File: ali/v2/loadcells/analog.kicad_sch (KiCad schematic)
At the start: 40 parts, among them J10 Conn_01x04, J11 Conn_01x04, J12 Conn_01x04, J9 Conn_01x04, U6 ADS124S08

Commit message: Small cleanups
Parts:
- R30: value 1k -> 4.7k; MPN RT0603BRD071KL -> RT0603BRD074K7L
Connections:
- net at C38.2, C39.1, R25.2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: now also D9.1 (A1)
- net at C34.1, C35.2, R22.2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: now also D6.1 (A1)
- net at J9.3 (Pin_3), R23.1: no longer D7.1 (A1)
- net at C35.1, C36.2, R23.2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: now also D7.1 (A1)
- net at J11.2 (Pin_2), R26.1: no longer D10.1 (A1)
- net at J11.3 (Pin_3), R27.1: no longer D11.1 (A1)
- net at J12.2 (Pin_2), R28.1: no longer D12.1 (A1)
- net at C45.1, C47.2, R28.2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: now also D12.1 (A1)
- net at C37.1, C39.2, R24.2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: now also D8.1 (A1)
- net at J10.3 (Pin_3), R25.1: no longer D9.1 (A1)
- net at J12.3 (Pin_3), R29.1: no longer D13.1 (A1)
- net at C43.2, C44.1, R27.2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: now also D11.1 (A1)
- net at J9.2 (Pin_2), R22.1: no longer D6.1 (A1)
- net at J10.2 (Pin_2), R24.1: no longer D8.1 (A1)
- net at C46.2, C47.1, R29.2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: now also D13.1 (A1)
- net at C42.1, C44.2, R26.2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: now also D10.1 (A1)
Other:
- moved on the sheet: C34, C35, C36, C37, C38, C39, C42, C43, C44, C45, C46, C47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

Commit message: Big changes (Tim and Daniel review part 1)
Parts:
- removed D10, D11, D12, D13, D6, D7, D8, D9: VTVS28ASMF, Diode_SMD:D_SMF, symbol Diode:SMF5V0A
- added C49: 1nF, APRL_Passive:C_0603, symbol Device:C_Small
- added C50: 10nF, APRL_Passive:C_0603, symbol Device:C_Small
- added R31: 4.7k, APRL_Passive:R_0603, symbol Device:R_Small_US
- C48: value 10nF -> 1nF; MPN GRM1885C1H103JA01 -> GRM1885C1H102FA01
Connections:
- net GND: now also C48.2, C49.1, R31.1; no longer C48.1, U6.29 (REFN0)
- net at R30.2, U6.30 (REFP0): now also C48.1, C50.2; no longer C48.2
- new net: C49.2, C50.1, R31.2, U6.29 (REFN0)
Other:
- moved on the sheet: C60, C61, C62, C63, C64, U6

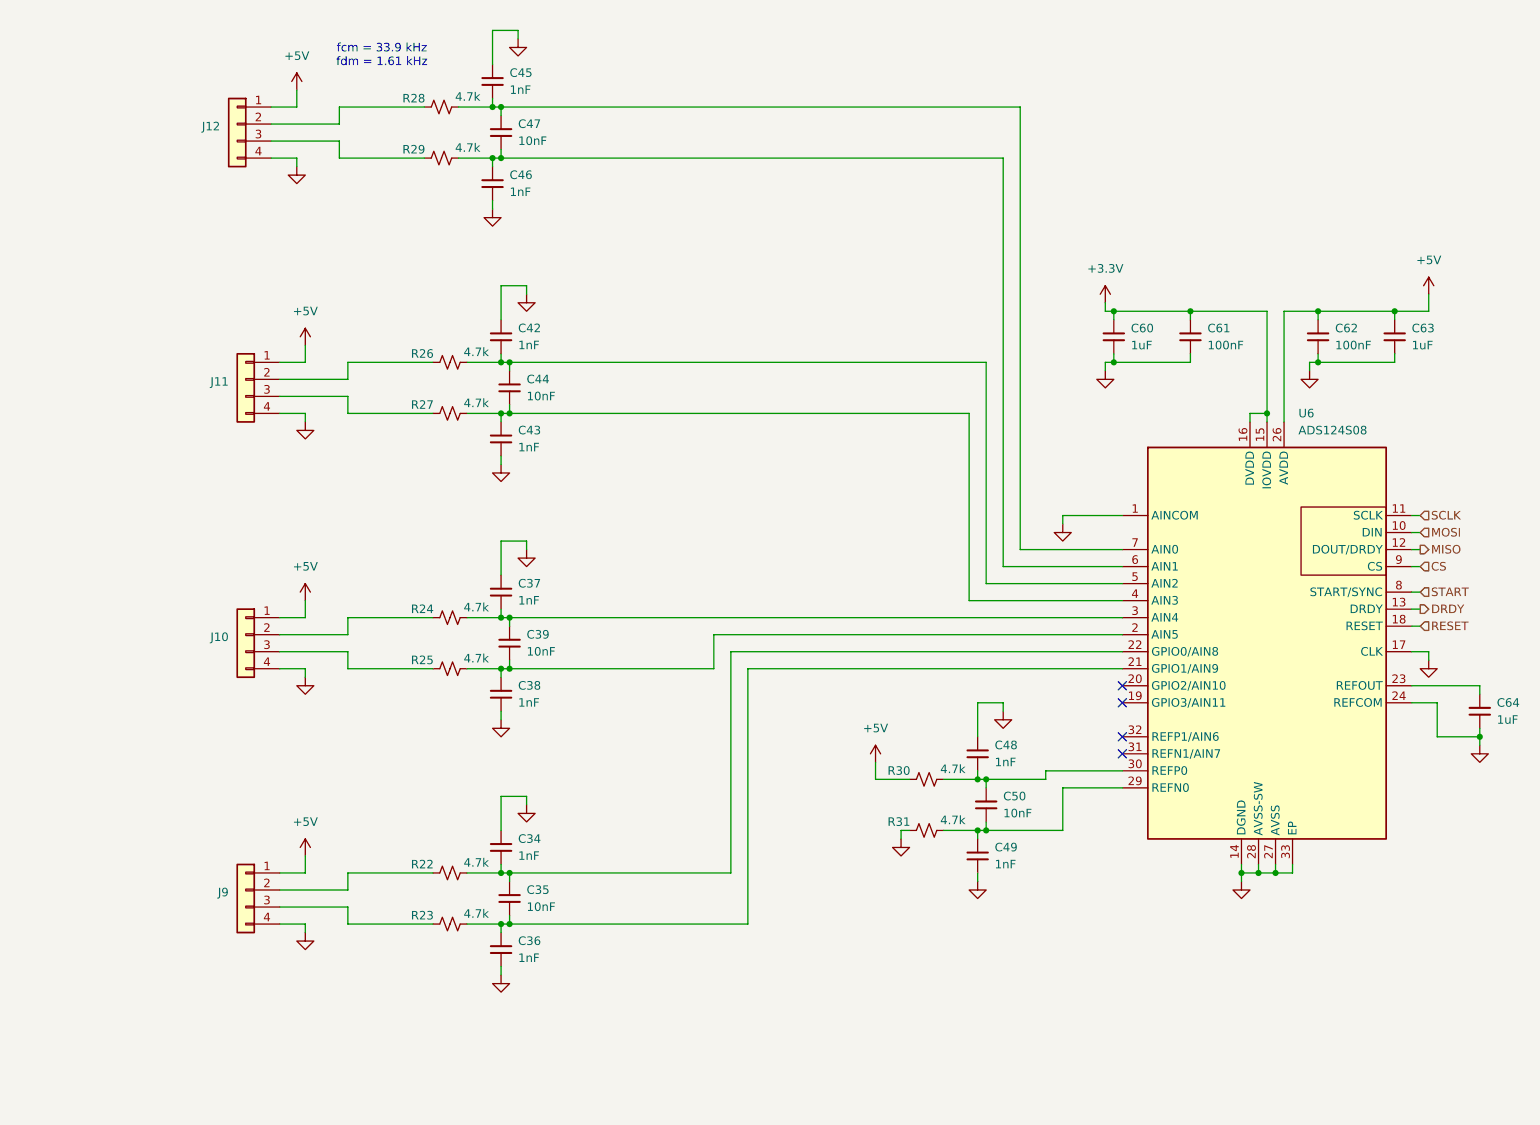
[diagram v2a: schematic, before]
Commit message: Update LCs to have 6 inputs instead of 4
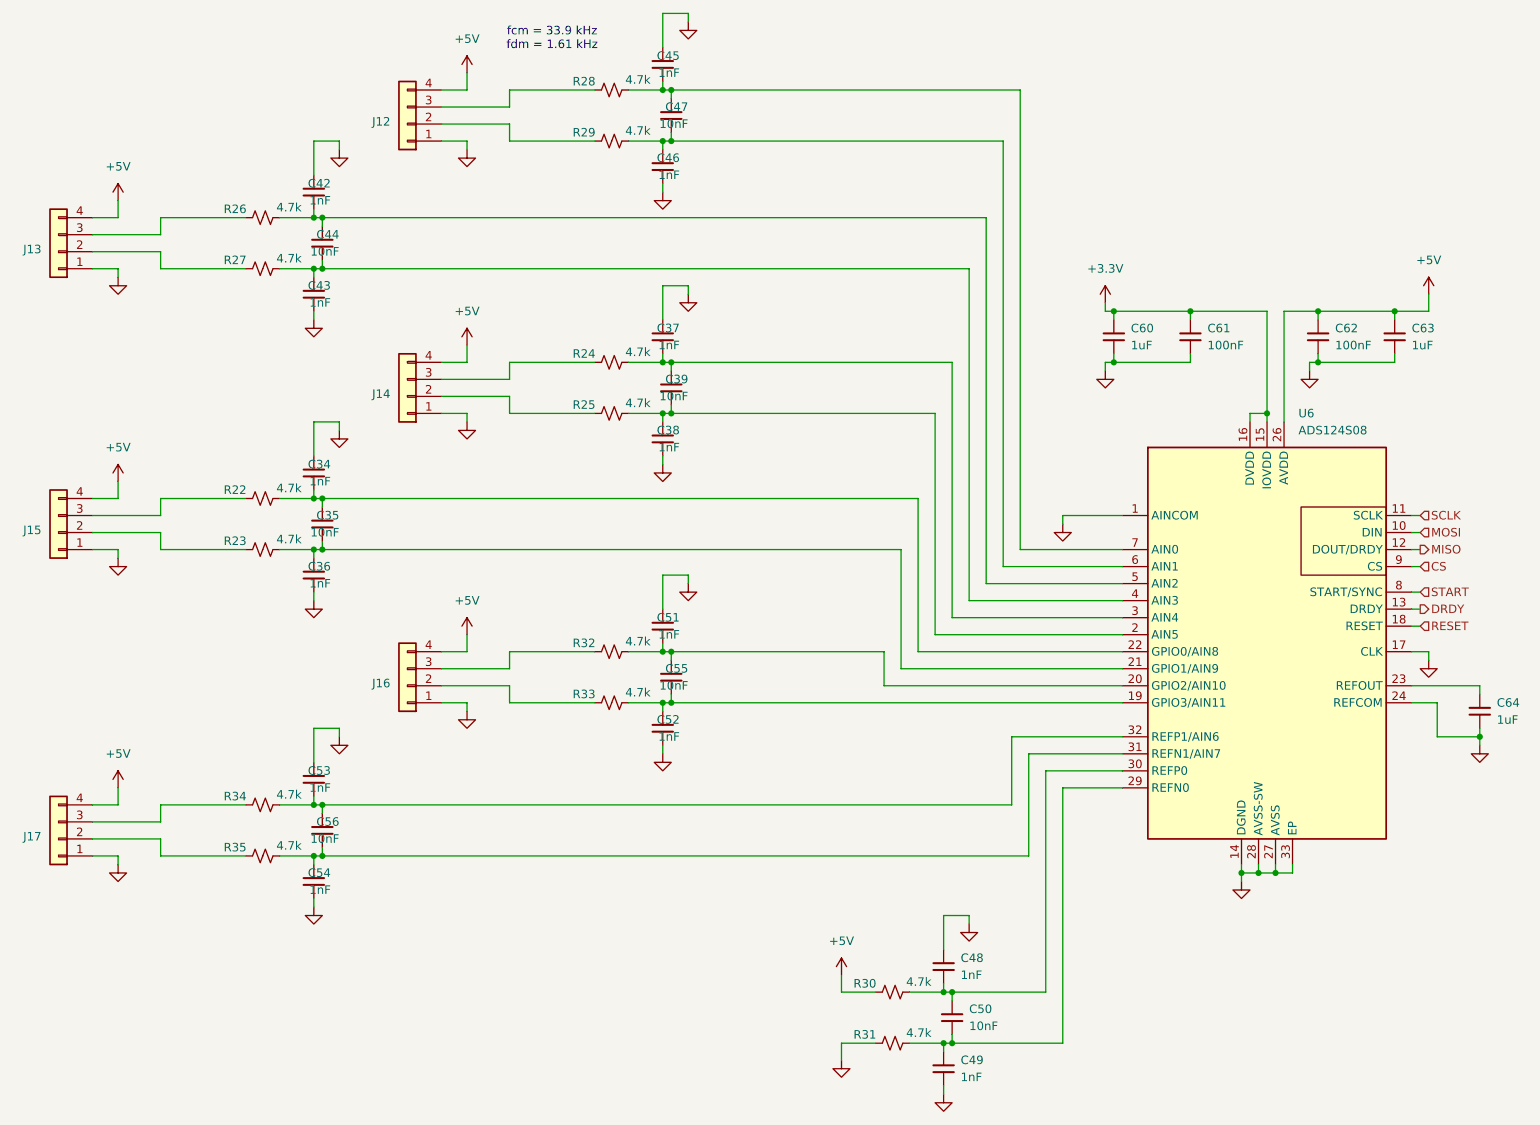
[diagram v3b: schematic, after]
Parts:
- removed J10, J11, J9: Conn_01x04, APRL_Connector_Molex:Molex_CLIK-Mate_503159-0401_1x04-1MP_P1.50mm_Vertical, symbol Connector_Generic:Conn_01x04
- added C51, C52, C53, C54: 1nF, APRL_Passive:C_0603, symbol Device:C_Small
- added C55, C56: 10nF, APRL_Passive:C_0603, symbol Device:C_Small
- added J13, J14, J15, J16, J17: Conn_01x04, APRL_Connector_Molex:Molex_CLIK-Mate_503159-0401_1x04-1MP_P1.50mm_Vertical, symbol Connector_Generic:Conn_01x04
- added R32, R33, R34, R35: 4.7k, APRL_Passive:R_0603, symbol Device:R_Small_US
- U6: symbol APRL_Analog:ADS124S08 -> APRL_Analog:ADS124S08-SEQPINS
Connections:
- net +5V: now also J12.4 (Pin_4), J13.4 (Pin_4), J14.4 (Pin_4), J15.4 (Pin_4), J16.4 (Pin_4), J17.4 (Pin_4); no longer J12.1 (Pin_1)
- net GND: now also C34.1, C36.2, C37.1, C38.2, C42.1, C43.2, C45.1, C46.2, J12.1 (Pin_1), C51.1, C52.2, C53.1, C54.2, J13.1 (Pin_1), J14.1 (Pin_1), J15.1 (Pin_1), J16.1 (Pin_1), J17.1 (Pin_1); no longer C34.2, C36.1, C37.2, C38.1, C42.2, C43.1, C45.2, C46.1, J12.4 (Pin_4)
- net at R25.2, U6.2 (AIN5): now also C38.1, C39.2; no longer C38.2, C39.1
- net at R22.2, U6.22 (GPIO0/AIN8): now also C34.2, C35.1; no longer C34.1, C35.2
- net at R23.1: now also J15.2 (Pin_2)
- net at R23.2, U6.21 (GPIO1/AIN9): now also C35.2, C36.1; no longer C35.1, C36.2
- net at R26.1: now also J13.3 (Pin_3)
- net at R27.1: now also J13.2 (Pin_2)
- net at R28.1: now also J12.3 (Pin_3); no longer J12.2 (Pin_2)
- net at R28.2, U6.7 (AIN0): now also C45.2, C47.1; no longer C45.1, C47.2
- net at R24.2, U6.3 (AIN4): now also C37.2, C39.1; no longer C37.1, C39.2
- net at R25.1: now also J14.2 (Pin_2)
- net at R29.1: now also J12.2 (Pin_2); no longer J12.3 (Pin_3)
- net at R27.2, U6.4 (AIN3): now also C43.1, C44.2; no longer C43.2, C44.1
- net at R22.1: now also J15.3 (Pin_3)
- net at R24.1: now also J14.3 (Pin_3)
- net at R29.2, U6.6 (AIN1): now also C46.1, C47.2; no longer C46.2, C47.1
- net at R26.2, U6.5 (AIN2): now also C42.2, C44.1; no longer C42.1, C44.2
- net at U6.19 (GPIO3/AIN11): now also C52.1, C55.2, R33.2
- net at U6.20 (GPIO2/AIN10): now also C51.2, C55.1, R32.2
- net at U6.31 (REFN1/AIN7): now also C54.1, C56.2, R35.2
- net at U6.32 (REFP1/AIN6): now also C53.2, C56.1, R34.2
- new net: J17.3 (Pin_3), R34.1
- new net: J16.2 (Pin_2), R33.1
- new net: J16.3 (Pin_3), R32.1
- new net: J17.2 (Pin_2), R35.1
- no-connect marks 4 -> 0
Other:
- moved on the sheet: C34, C35, C36, C37, C38, C39, C42, C43, C44, C45, C46, C47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

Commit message: Use 1206 on AFEs
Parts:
- C35, C39, C44, C47, C50, C55, C56: footprint APRL_Passive:C_0603 -> APRL_Passive:C_1206
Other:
- moved on the sheet: C48, C49, C50, R30, R31
